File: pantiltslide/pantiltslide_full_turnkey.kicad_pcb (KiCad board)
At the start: 4 copper layers, 89.5 x 113 mm, 53 parts, among them J1 Conn_01x22_Socket, J17 Motor_Slide, J18 Motor_Pan, J19 Motor_Tilt, J2 Conn_01x22_Socket, J20 TCA9548A_Mux, J21 AS5600_Pan, J22 AS5600_Tilt, J23 OLED, J24 TCA9548A_Mux, J26 Limit_Min, J27 Limit_Max, J28 Motor_Aux, J29 Enc_Slide, J30 Enc_Pan, J31 Enc_Tilt, J32 Enc_Aux, J33 Btn_SetKeyframe, J34 Btn_ClearKeyframe, J35 Btn_PlayPause, J36 Btn_Reset, J37 5V_In, J38 24V_In, U1 tmc2209, U2 tmc2209, U3 tmc2209, U4 tmc2209

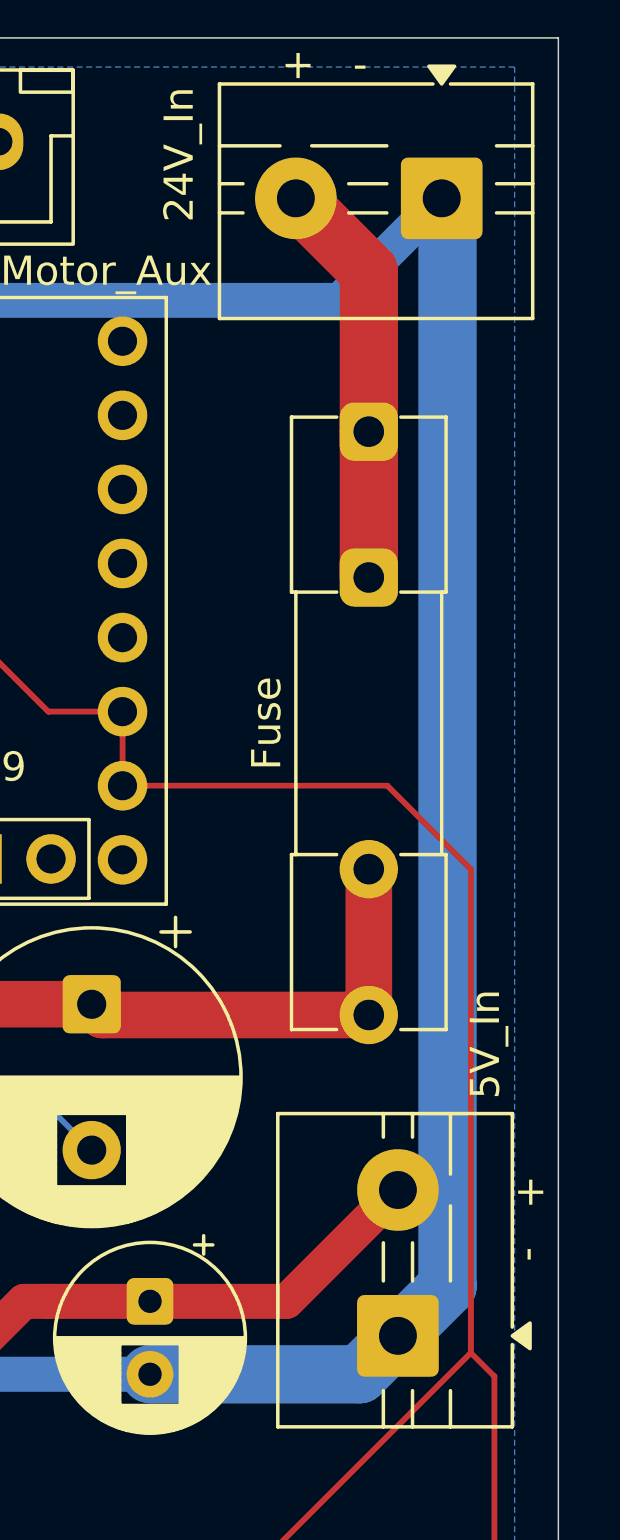
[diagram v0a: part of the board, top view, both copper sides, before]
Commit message: fixing uart, and adjusting pins
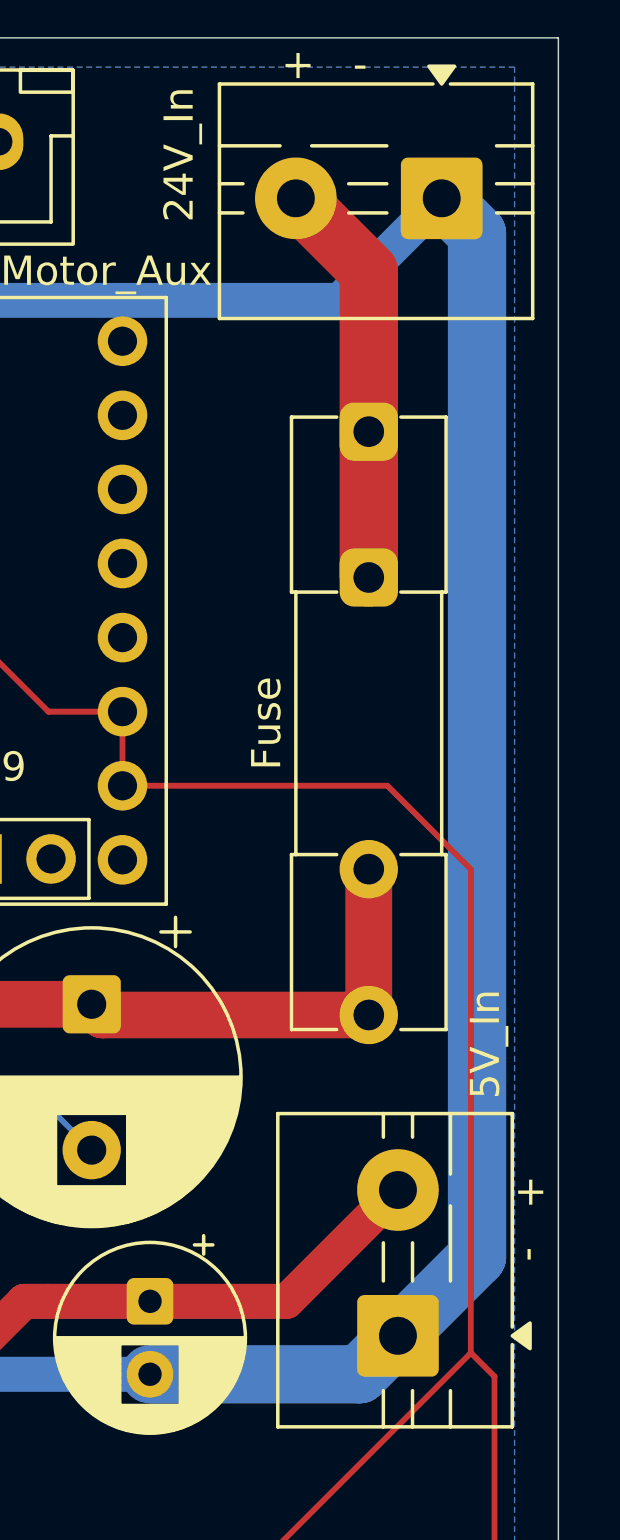
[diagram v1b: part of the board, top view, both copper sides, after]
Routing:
- net GND: track 824.9 -> 825.8 mm
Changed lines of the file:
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@@
-	)
-	(segment
-		(start 171.2 60.8)
-		(end 171.2 23.7)
-		(width 2)
-		(layer "B.Cu")
-		(net "GND")
 	)
 	(segment
@@
 	)
 	(segment
+		(start 169.5 62.5)
+		(end 172.212 59.788)
+		(width 2)
+		(layer "B.Cu")
+		(net "GND")
+	)
+	(segment
 		(start 102.5 79)
 		(end 109.755 79)
 		(width 0.2)
+		(layer "B.Cu")
+		(net "GND")
+	)
+	(segment
+		(start 172.212 59.788)
+		(end 172.212 24.712)
+		(width 2)
 		(layer "B.Cu")
 		(net "GND")
@@
 	)
 	(segment
-		(start 169.5 62.5)
-		(end 171.2 60.8)
-		(width 2)
-		(layer "B.Cu")
-		(net "GND")
-	)
-	(segment
 		(start 90 84.25)
 		(end 88.7 85.55)
@@
 		(layer "B.Cu")
 		(net "GND")
+	)
+	(segment
+		(start 172.212 24.712)
+		(end 171.2 23.7)
+		(width 2)
+		(layer "B.Cu")
+		(net "GND")

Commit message: more corrections and refinements before prod
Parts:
- added J41: Aux_Max, Connector_JST:JST_XH_B2B-XH-A_1x02_P2.50mm_Vertical, F.Cu at (102.6, 119.9)
- added R10: 100R, Resistor_SMD:R_0603_1608Metric, F.Cu at (118.4, 89.6)
- added R11: 100R, Resistor_SMD:R_0603_1608Metric, F.Cu at (109.7, 112.8)
- added R12: 1k R, Resistor_SMD:R_0603_1608Metric, F.Cu at (118.4, 92.8)
- moved C12 17.1 mm to (159.1, 126.6)
- moved C14 3.97 mm to (145.0, 126.5)
- moved C15 3.97 mm to (148.5, 126.5)
- moved C16 3.97 mm to (152.0, 126.5)
- moved C17 3.97 mm to (155.5, 126.5)
- moved C13 3.51 mm to (142.0, 126.5)
- moved R8 1.25 mm to (170.4, 110.0)
- moved C9 0.64 mm to (88.1, 51.1)
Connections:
- J33 pad 1: GPIO_1 -> GPIO_48
- U1 pad 11: GPIO_42 -> UART
- U1 pad 12: GPIO_41 -> unconnected-(U1-UART-Pad12)
- U2 pad 11: GPIO_42 -> UART
- U2 pad 12: GPIO_41 -> unconnected-(U2-UART-Pad12)
- U3 pad 11: GPIO_42 -> UART
- U3 pad 12: GPIO_41 -> unconnected-(U3-UART-Pad12)
- U4 pad 10: GPIO_47 -> GPIO_1
- U4 pad 11: GPIO_42 -> UART
- U4 pad 12: GPIO_41 -> unconnected-(U4-UART-Pad12)
- U4 pad 9: GPIO_48 -> GPIO_2
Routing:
- net UART: track 0.00 -> 206.6 mm, vias 0 -> 1
- net GPIO_42: track 188.9 -> 11.9 mm
- net GPIO_41: track 164.2 -> 2.60 mm
- net GPIO_2: track 0.00 -> 130.3 mm, vias 0 -> 1
- net GND: track 825.8 -> 936.5 mm
- net GPIO_1: track 48.3 -> 119.7 mm, vias 0 -> 1
- net GPIO_47: track 75.5 -> 7.34 mm, vias 1 -> 0
- net GPIO_48: track 87.6 -> 25.7 mm, vias 1 -> 0
- net GPIO_13: track 68.7 -> 71.9 mm
- net 3.3v: track 544.7 -> 547.0 mm
- net MUX_CH1_SCL: track 39.9 -> 38.1 mm
- net Net-(R10-Pad2): track 0.00 -> 1.52 mm
- net GPIO_14: track 67.0 -> 68.5 mm
- net GPIO_40: track 40.4 -> 41.3 mm
- net +24V: track 129.3 -> 128.5 mm

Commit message: pcb update
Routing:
- net SLIDE_M1A: track 16.2 -> 17.6 mm
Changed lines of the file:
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@@
 	)
 	(segment
-		(start 86.5 34.37)
-		(end 86.5 24.21)
+		(start 88.15 36.02)
+		(end 92.456 31.714)
 		(width 1.2)
-		(layer "In1.Cu")
+		(layer "In2.Cu")
 		(net "SLIDE_M1A")
 	)
 	(segment
-		(start 86.5 24.21)
-		(end 89.15 21.56)
+		(start 92.456 31.714)
+		(end 92.456 24.866)
 		(width 1.2)
-		(layer "In1.Cu")
+		(layer "In2.Cu")
 		(net "SLIDE_M1A")
 	)
 	(segment
-		(start 88.15 36.02)
-		(end 86.5 34.37)
+		(start 92.456 24.866)
+		(end 89.15 21.56)
 		(width 1.2)
-		(layer "In1.Cu")
+		(layer "In2.Cu")
 		(net "SLIDE_M1A")
 	)

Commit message: udpates
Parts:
- added REF**: PinSocket_1x08_P2.54mm_Vertical, Connector_PinSocket_2.54mm:PinSocket_1x08_P2.54mm_Vertical, F.Cu at (160.1, 28.4)
- added REF**: PinSocket_1x08_P2.54mm_Vertical, Connector_PinSocket_2.54mm:PinSocket_1x08_P2.54mm_Vertical, F.Cu at (140.6, 28.4)
- added REF**: PinSocket_1x08_P2.54mm_Vertical, Connector_PinSocket_2.54mm:PinSocket_1x08_P2.54mm_Vertical, F.Cu at (107.7, 28.4)
- added REF**: PinSocket_1x08_P2.54mm_Vertical, Connector_PinSocket_2.54mm:PinSocket_1x08_P2.54mm_Vertical, F.Cu at (120.3, 28.4)
- added REF**: PinSocket_1x08_P2.54mm_Vertical, Connector_PinSocket_2.54mm:PinSocket_1x08_P2.54mm_Vertical, F.Cu at (88.2, 28.4)
- added REF**: PinSocket_1x08_P2.54mm_Vertical, Connector_PinSocket_2.54mm:PinSocket_1x08_P2.54mm_Vertical, F.Cu at (147.4, 28.4)
- added REF**: PinSocket_1x08_P2.54mm_Vertical, Connector_PinSocket_2.54mm:PinSocket_1x08_P2.54mm_Vertical, F.Cu at (127.9, 28.4)
- added REF**: PinSocket_1x08_P2.54mm_Vertical, Connector_PinSocket_2.54mm:PinSocket_1x08_P2.54mm_Vertical, F.Cu at (100.9, 28.4)
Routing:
- net UART: track 206.6 -> 335.2 mm
- net GPIO_40: track 41.3 -> 22.7 mm
- net GPIO_2: track 130.3 -> 127.1 mm
- net 3.3v: track 547.0 -> 545.2 mm

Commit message: updates
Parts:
- removed REF** (x8): PinSocket_1x08_P2.54mm_Vertical, Connector_PinSocket_2.54mm:PinSocket_1x08_P2.54mm_Vertical
